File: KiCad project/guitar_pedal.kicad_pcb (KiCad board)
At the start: 2 copper layers, 68.6 x 114.3 mm, 54 parts, among them J1 NMJ6HCD2, J2 NMJ6HCD2, J3 AVR-ISP-6, SW1 SW_SPST, SW2 SWITCH_3PDT, U1 ATmega1284-P, U2 L7805, U3 TL061, U4 TL061, Y1 Crystal 16MHz

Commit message: Design review changes. Vias added, fixed capacitors in output stage.
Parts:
- D1: footprint LED_SMD:LED_0603_1608Metric -> LED_THT:LED_D3.0mm
- moved D1 35.4 mm to (154.9, 45.7), turned to 0 degrees
- moved RV1 2.58 mm to (149.9, 55.9)
- moved Y1 1.56 mm to (137.2, 78.7)
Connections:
- D1 pad 1: GND -> (no net)
- D1 pad 2: Net-(D1-A) -> (no net)
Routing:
- net GND: track 353.9 -> 342.3 mm, vias 8 -> 34
- net +5V: track 237.0 -> 231.9 mm
- net PA0: track 70.5 -> 66.2 mm
- net FX Out: track 28.3 -> 31.2 mm
- net Net-(D1-A): track 2.83 -> 0.00 mm
- net PA1: track 8.88 -> 6.52 mm
- net PD1: track 22.9 -> 24.4 mm
- net Net-(U3-+): track 35.1 -> 35.8 mm

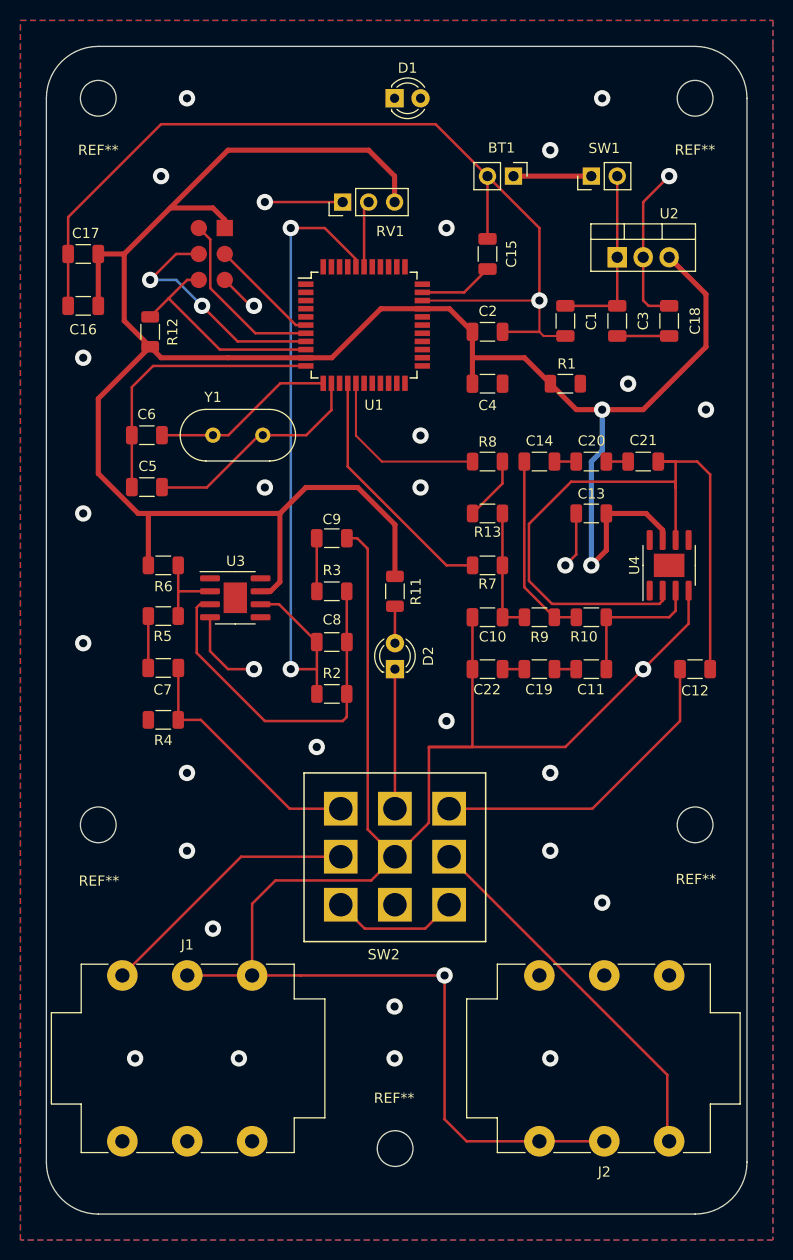
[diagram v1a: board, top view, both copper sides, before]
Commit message: Fixed cap series to parallel. Includes updated PCB and Gerber files
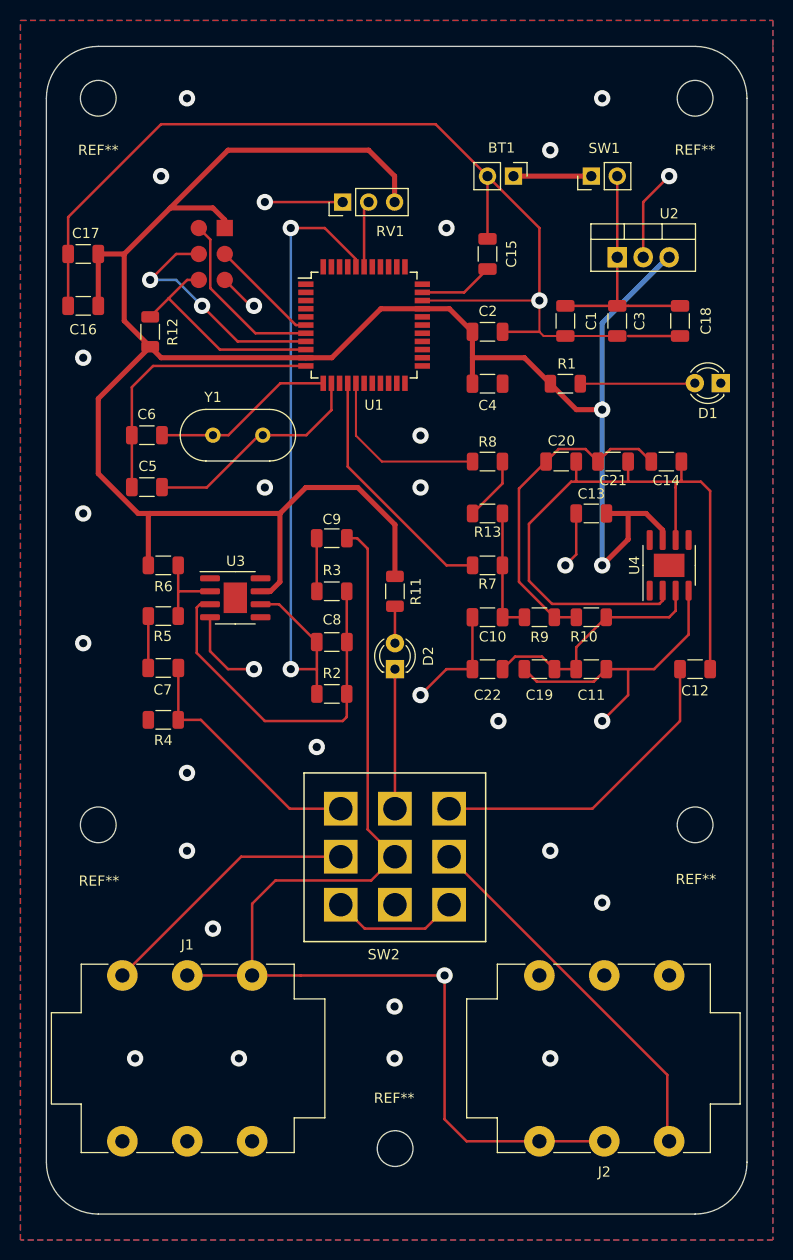
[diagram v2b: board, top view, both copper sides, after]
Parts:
- moved D1 42.4 mm to (186.9, 73.6), turned to 180 degrees
- moved C14 12.4 mm to (181.5, 81.3)
- moved C21 2.95 mm to (176.3, 81.3)
- moved C20 2.95 mm to (171.2, 81.3)
- moved C18 1.06 mm to (182.9, 67.5), turned to -90 degrees
- turned C11 to 0 degrees
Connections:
- C11 pad 2: Net-(C11-Pad2) -> GND
- C14 pad 1: Net-(C14-Pad1) -> Net-(U4--)
- C18 pad 1: Net-(C18-Pad1) -> Net-(SW1-B)
- C19 pad 1: Net-(C11-Pad2) -> Net-(U4-+)
- C19 pad 2: Net-(C19-Pad2) -> GND
- C20 pad 1: Net-(C20-Pad1) -> Net-(U4--)
- C20 pad 2: Net-(C14-Pad1) -> Net-(C14-Pad2)
- C21 pad 2: Net-(C20-Pad1) -> Net-(C14-Pad2)
- C22 pad 1: Net-(C19-Pad2) -> Net-(U4-+)
- C3 pad 2: Net-(C18-Pad1) -> GND
- D1 pad 1: (no net) -> GND
- D1 pad 2: (no net) -> Net-(D1-A)
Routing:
- net GND: track 342.3 -> 321.7 mm, vias 34 -> 32
- net Net-(C14-Pad2): track 18.6 -> 32.3 mm
- net Net-(D1-A): track 0.00 -> 10.9 mm
- net Net-(U4-+): track 14.1 -> 24.0 mm
- net Net-(SW1-B): track 17.8 -> 23.9 mm
- net +5V: track 231.9 -> 226.8 mm
- net Net-(C18-Pad1): track 5.08 -> 0.00 mm
- net Net-(C20-Pad1): track 2.13 -> 0.00 mm
- net Net-(C19-Pad2): track 2.13 -> 0.00 mm
- net Net-(C14-Pad1): track 2.13 -> 0.00 mm
- net Net-(C11-Pad2): track 2.13 -> 0.00 mm
- net Net-(U4--): track 71.4 -> 70.0 mm

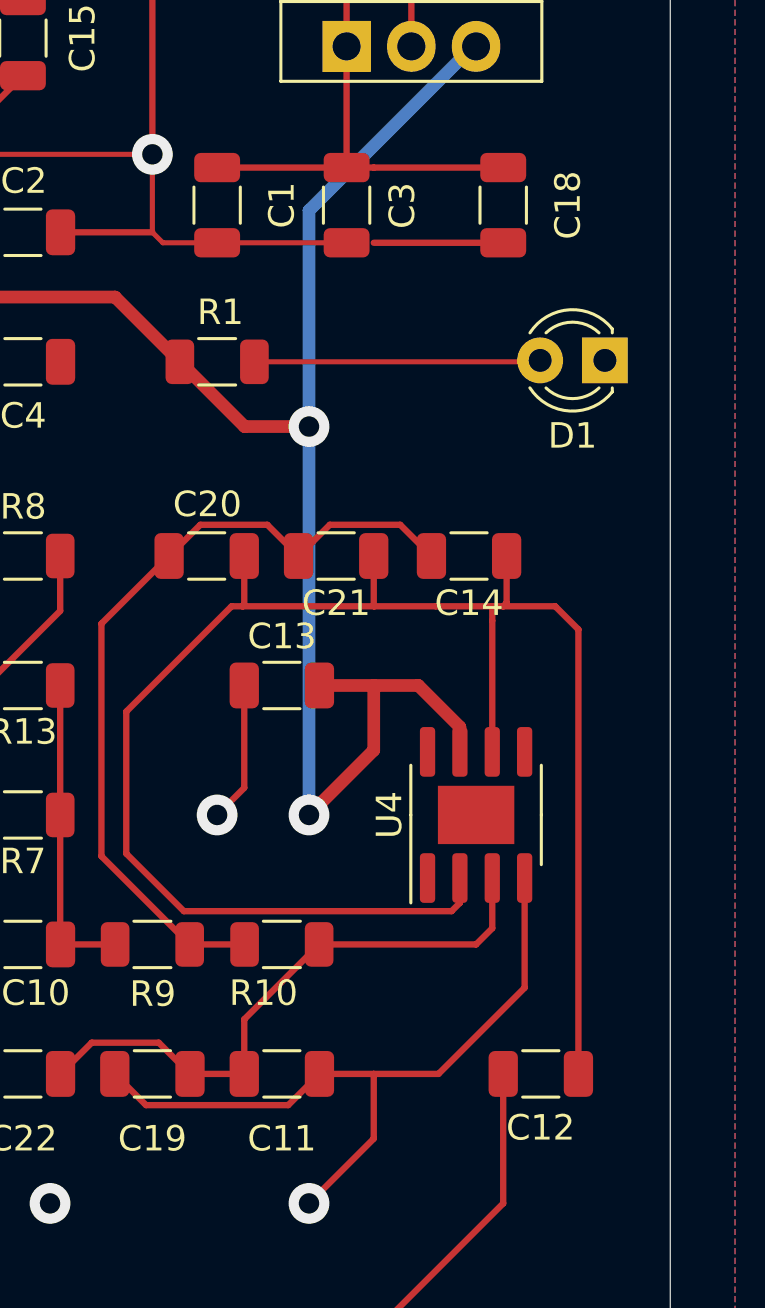
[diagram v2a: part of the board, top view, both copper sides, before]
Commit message: Minor fixes to silkscreen
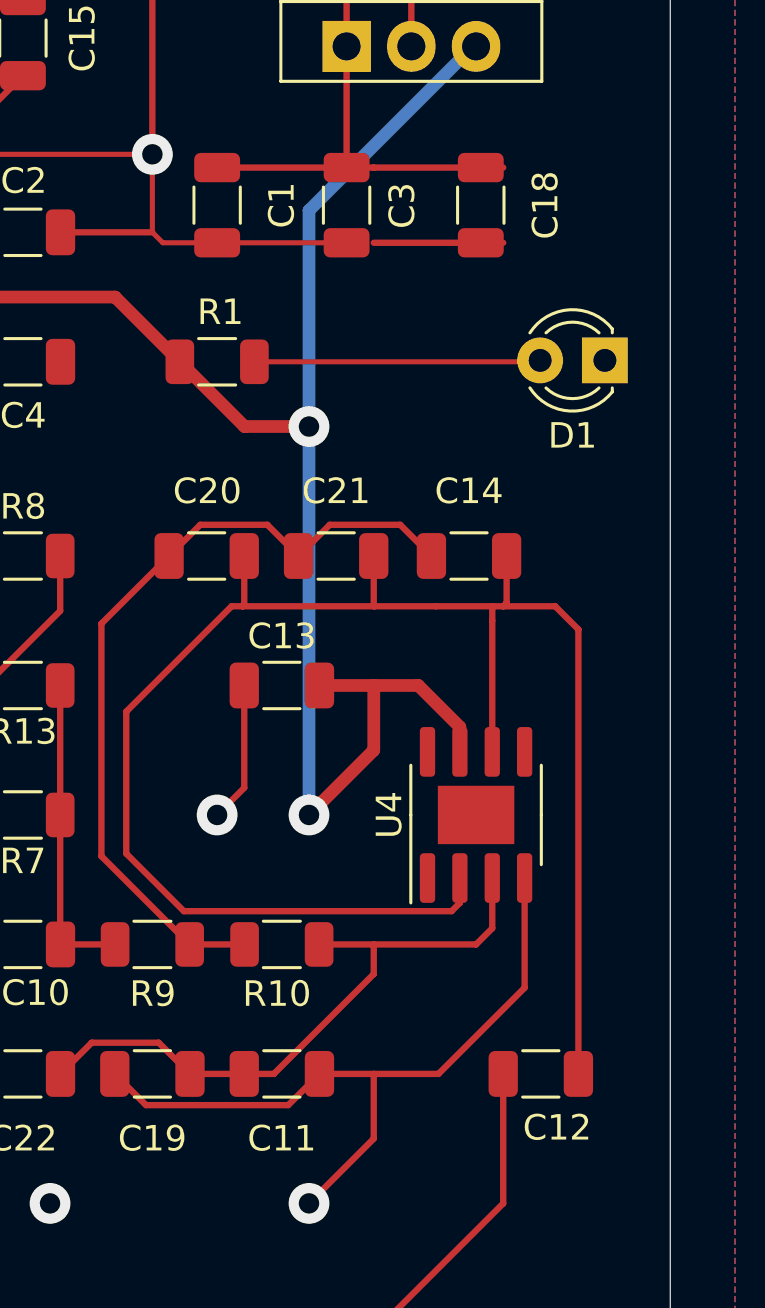
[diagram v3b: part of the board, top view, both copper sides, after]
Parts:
- moved C18 0.88 mm to (182.0, 67.5)
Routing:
- net Net-(U4-+): track 24.0 -> 25.5 mm
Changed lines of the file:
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@@
     (property "ki_keywords" "cap capacitor")
     (attr smd)
-    (fp_text reference "C14" (at 0 -1.85) (layer "F.SilkS")
+    (fp_text reference "C14" (at 0 2.54) (layer "F.SilkS")
         (effects (font (size 1 1) (thickness 0.15)))
     )
@@
     (property "ki_keywords" "cap capacitor")
     (attr smd)
-    (fp_text reference "C12" (at 0.009358 -2.112842) (layer "F.SilkS")
+    (fp_text reference "C12" (at -0.645 -2.112842) (layer "F.SilkS")
         (effects (font (size 1 1) (thickness 0.15)))
     )
@@
     (property "ki_keywords" "cap capacitor")
     (attr smd)
-    (fp_text reference "C21" (at 0 -1.85) (layer "F.SilkS")
+    (fp_text reference "C21" (at 0 2.54) (layer "F.SilkS")
         (effects (font (size 1 1) (thickness 0.15)))
     )
@@
     (property "ki_keywords" "R res resistor")
     (attr smd)
-    (fp_text reference "R10" (at 0.721301 -1.90843) (layer "F.SilkS")
+    (fp_text reference "R10" (at 0.195 -1.94447) (layer "F.SilkS")
         (effects (font (size 1 1) (thickness 0.15)))
     )
@@
   )
   (footprint "Capacitor_SMD:C_1206_3216Metric" (layer "F.Cu")
-    (at 182.88 67.515 -90)
+    (at 182 67.515 -90)
     (descr "Capacitor SMD 1206 (3216 Metric), square (rectangular) end terminal, IPC_7351 nominal, (Body size source: IPC-SM-782 page 76, https://www.pcb-3d.com/wordpress/wp-content/uploads/ipc-sm-782a_amendment_1_and_2.pdf), generated with kicad-footprint-generator")
     (tags "capacitor")
@@
     (property "ki_keywords" "cap capacitor")
     (attr smd)
-    (fp_text reference "C20" (at -0.026867 2.027278) (layer "F.SilkS")
+    (fp_text reference "C20" (at -0.026867 2.54) (layer "F.SilkS")
         (effects (font (size 1 1) (thickness 0.15)))
     )
@@
   (segment (start 152.307511 117.292512) (end 152.307511 89.815011) (width 0.25) (layer "F.Cu") (net 1))
   (segment (start 180.34 101.6) (end 183.72 98.22) (width 0.25) (layer "F.Cu") (net 1))
+  (segment (start 177.8 68.99) (end 182.88 68.99) (width 0.25) (layer "F.Cu") (net 1))
   (segment (start 169.115 58.42) (end 169.115 65.52) (width 0.25) (layer "F.Cu") (net 1))
   (segment (start 164.035 59.485) (end 164.035 53.34) (width 0.25) (layer "F.Cu") (net 1))
@@
   (segment (start 160.02 101.6) (end 162.56 101.6) (width 0.25) (layer "F.Cu") (net 1))
   (segment (start 138.315 63.5) (end 140.855 66.04) (width 0.25) (layer "F.Cu") (net 1))
-  (segment (start 177.8 68.99) (end 182.88 68.99) (width 0.25) (layer "F.Cu") (net 1))
   (segment (start 158.955 48.26) (end 164.035 53.34) (width 0.25) (layer "F.Cu") (net 1))
   (segment (start 122.985 57.355) (end 132.08 48.26) (width 0.25) (layer "F.Cu") (net 1))
@@
   (segment (start 176.735 61.285) (end 176.735 53.34) (width 0.25) (layer "F.Cu") (net 43))
   (segment (start 176.735 66.04) (end 176.735 61.285) (width 0.25) (layer "F.Cu") (net 43))
+  (segment (start 177.8 66.04) (end 171.655 66.04) (width 0.25) (layer "F.Cu") (net 43))
   (segment (start 182.88 66.04) (end 177.8 66.04) (width 0.25) (layer "F.Cu") (net 43))
-  (segment (start 177.8 66.04) (end 171.655 66.04) (width 0.25) (layer "F.Cu") (net 43))
   (segment (start 130.835 101.4725) (end 130.8225 101.485) (width 0.25) (layer "F.Cu") (net 44))
   (segment (start 130.835 96.405) (end 130.835 101.4725) (width 0.25) (layer "F.Cu") (net 44))
@@
   (segment (start 165.4975 91.44) (end 165.4975 96.5075) (width 0.25) (layer "F.Cu") (net 50))
   (segment (start 165.4975 86.36) (end 165.4975 91.44) (width 0.25) (layer "F.Cu") (net 50))
+  (segment (start 177.8 97.681826) (end 177.8 96.52) (width 0.25) (layer "F.Cu") (net 51))
   (segment (start 166.735 100.375) (end 169.365 100.375) (width 0.25) (layer "F.Cu") (net 51))
   (segment (start 172.72 101.6) (end 170.59 101.6) (width 0.25) (layer "F.Cu") (net 51))
-  (segment (start 172.72 99.4575) (end 175.6575 96.52) (width 0.25) (layer "F.Cu") (net 51))
   (segment (start 165.51 101.6) (end 166.735 100.375) (width 0.25) (layer "F.Cu") (net 51))
-  (segment (start 172.72 101.6) (end 172.72 99.4575) (width 0.25) (layer "F.Cu") (net 51))
+  (segment (start 173.881826 101.6) (end 177.8 97.681826) (width 0.25) (layer "F.Cu") (net 51))
+  (segment (start 172.72 101.6) (end 173.881826 101.6) (width 0.25) (layer "F.Cu") (net 51))
   (segment (start 165.51 101.6) (end 165.1 101.6) (width 0.25) (layer "F.Cu") (net 51))
   (segment (start 182.45 95.885) (end 181.815 96.52) (width 0.25) (layer "F.Cu") (net 51))
